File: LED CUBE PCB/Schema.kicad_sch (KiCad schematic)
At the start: 4 parts

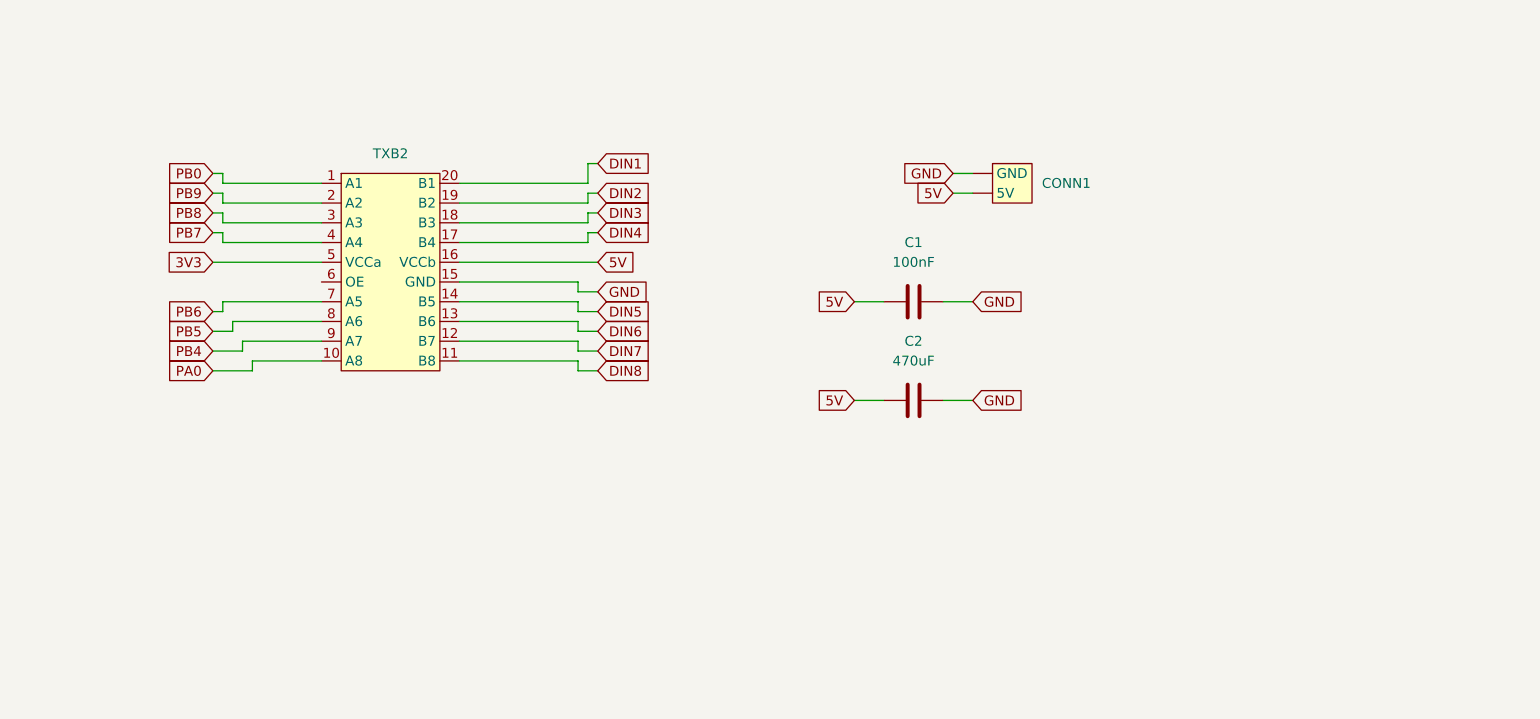
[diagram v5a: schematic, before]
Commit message: Corrected schema after review by Borna (Marina)
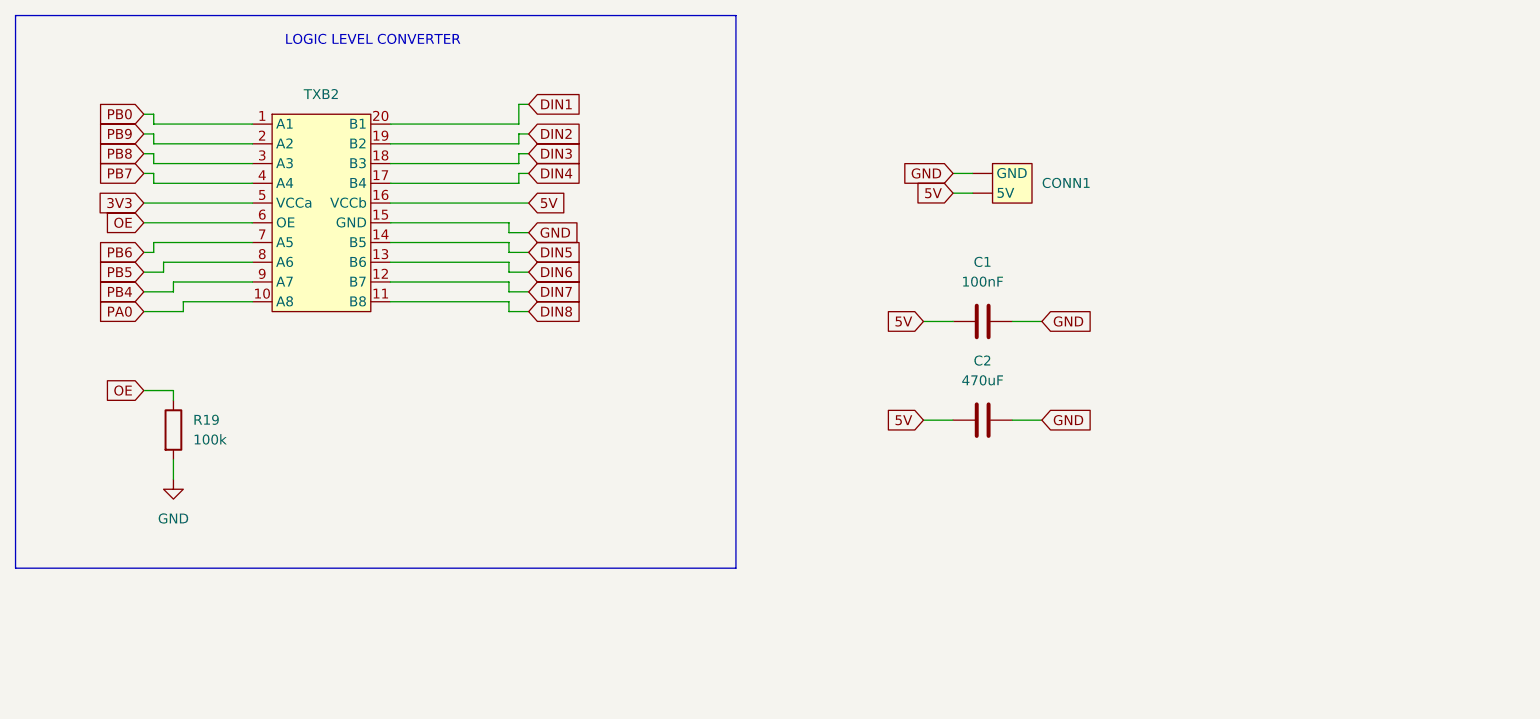
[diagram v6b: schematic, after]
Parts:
- added R19: 100k, BornaKiCad:R0603, symbol Device:R
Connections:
- net GND: now also R19.2
- net OE: now reaches TXB2.6 (OE)
- net OE: now also R19.1
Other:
- note added: "LOGIC LEVEL CONVERTER"
- moved on the sheet: C1, C2, TXB2

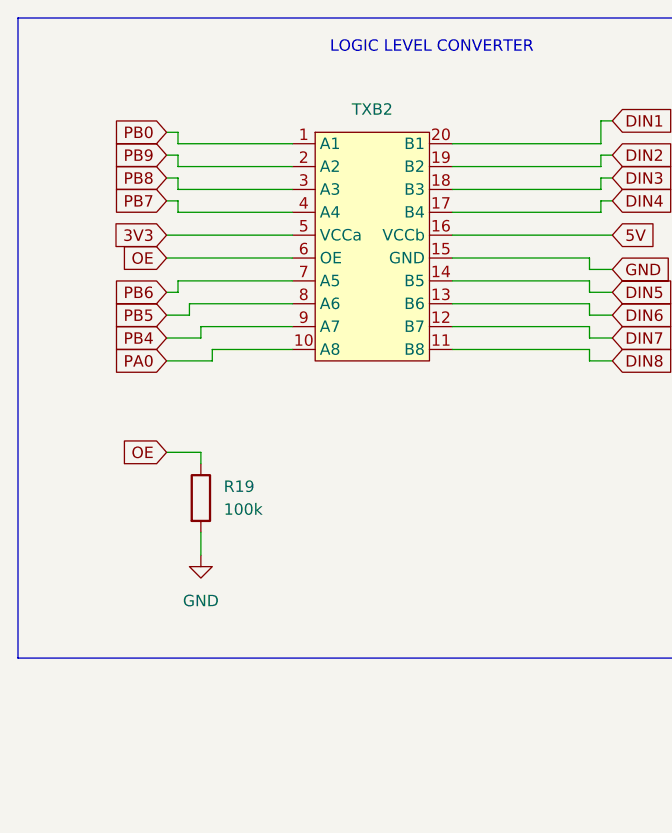
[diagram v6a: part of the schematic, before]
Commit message: Replaced symbol for TXB and STM
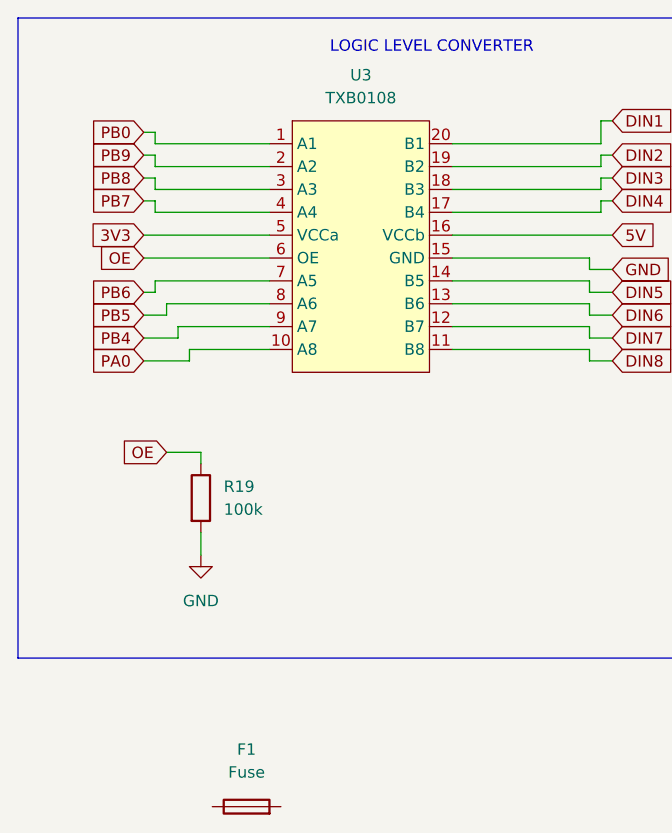
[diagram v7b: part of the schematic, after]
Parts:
- removed TXB2: ~, TXB0108:TXB0108, symbol TXB0108:TXB0108
- added F1: Fuse, symbol Device:Fuse
- added U3: TXB0108, TXB0108:TXB0108, symbol Marina_Library:TXB0108
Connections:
- net 3V3: now also U3.5 (VCCa)
- net 5V: now also U3.16 (VCCb)
- net DIN1: now also U3.20 (B1)
- net DIN2: now also U3.19 (B2)
- net DIN3: now also U3.18 (B3)
- net DIN4: now also U3.17 (B4)
- net DIN5: now also U3.14 (B5)
- net DIN6: now also U3.13 (B6)
- net DIN7: now also U3.12 (B7)
- net DIN8: now also U3.11 (B8)
- net GND: now also U3.15 (GND)
- net OE: now also U3.6 (OE)
- net PA0: now also U3.10 (A8)
- net PB0: now also U3.1 (A1)
- net PB4: now also U3.9 (A7)
- net PB5: now also U3.8 (A6)
- net PB6: now also U3.7 (A5)
- net PB7: now also U3.4 (A4)
- net PB8: now also U3.3 (A3)
- net PB9: now also U3.2 (A2)

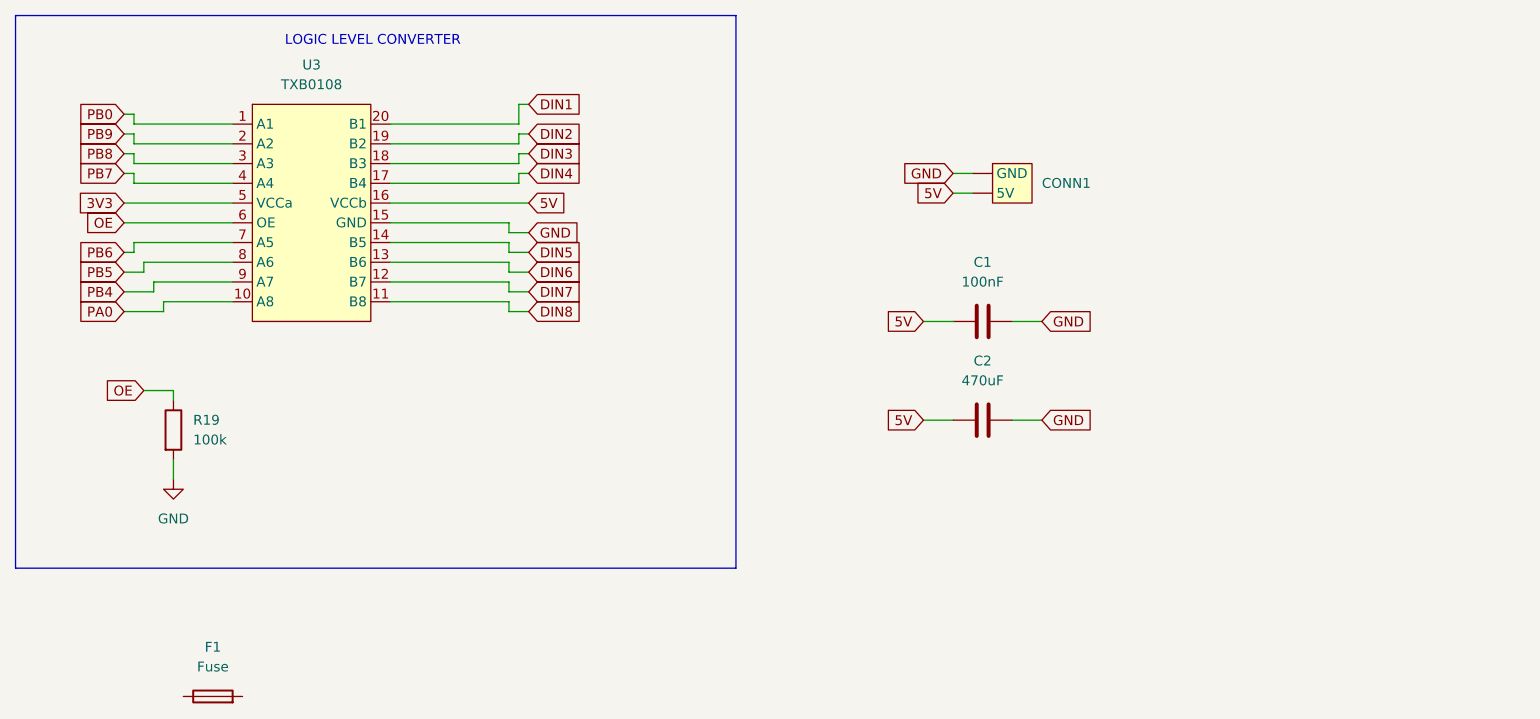
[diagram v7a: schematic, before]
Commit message: Added fuse and bat20
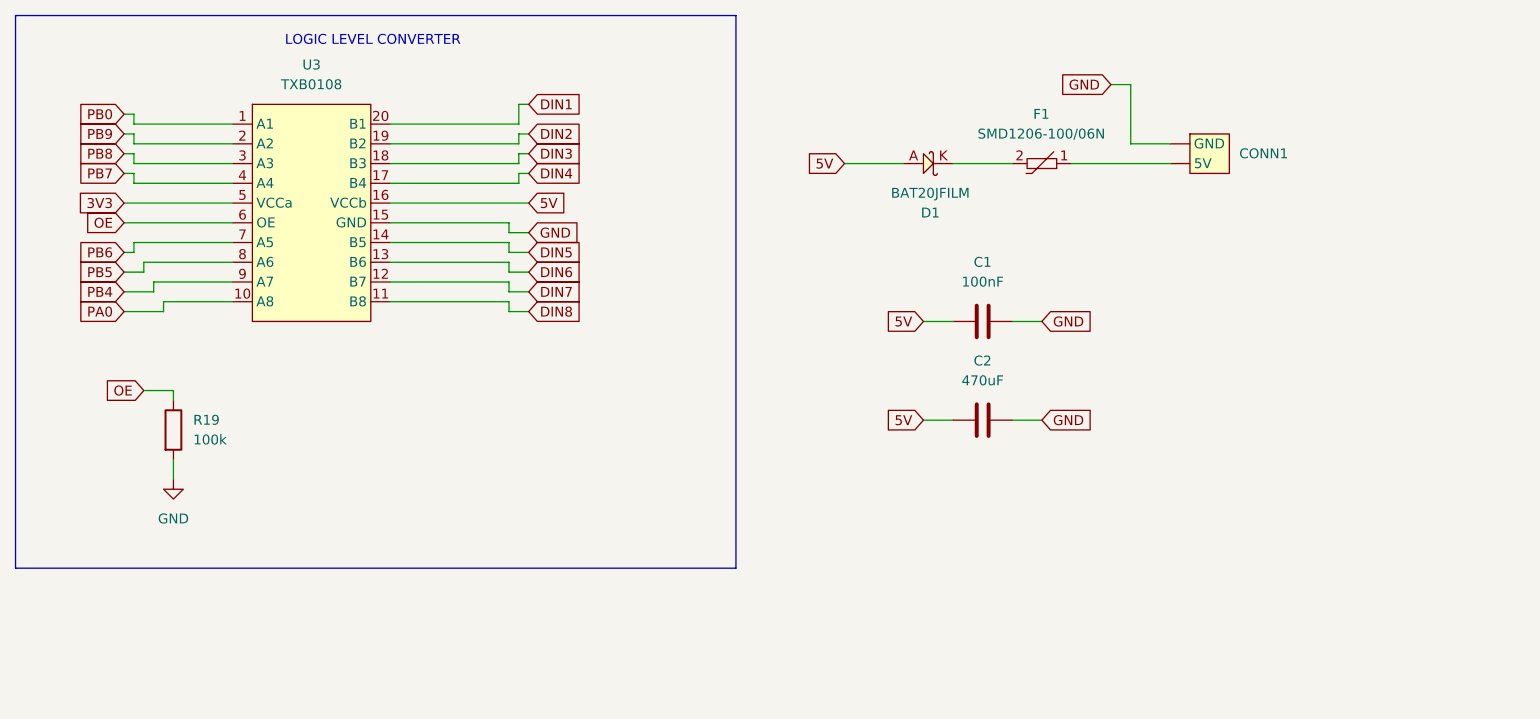
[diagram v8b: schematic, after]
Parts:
- removed F1: Fuse, symbol Device:Fuse
- added D1: BAT20JFILM, Borna KiCAD Library:SOD323, symbol Borna KiCAD Library:BAT20JFILM
- added F1: SMD1206-100/06N, Borna KiCAD Library:1206, symbol Borna KiCAD Library:SMD1206-100/06N
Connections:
- net 5V: now also D1.A; no longer CONN1. (GND)
- new net: D1.K, F1.2
- new net: CONN1. (GND), F1.1
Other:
- moved on the sheet: CONN1
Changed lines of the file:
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@@
+	(wire
+		(pts
+			(xy 160.02 30.48) (xy 160.02 22.86)
+		)
+		(stroke
+			(width 0)
+			(type default)
+		)
+	)
 	(wire
 		(pts
@@
 	(wire
 		(pts
-			(xy 137.16 36.83) (xy 139.7 36.83)
+			(xy 160.02 22.86) (xy 157.48 22.86)
 		)
 		(stroke
@@
 	(wire
 		(pts
+			(xy 160.02 30.48) (xy 165.1 30.48)
+		)
+		(stroke
+			(width 0)
+			(type default)
+		)
+	)
+	(wire
+		(pts
 			(xy 30.48 52.07) (xy 35.56 52.07)
 		)
@@
 	(wire
 		(pts
+			(xy 152.4 33.02) (xy 165.1 33.02)
+		)
+		(stroke
+			(width 0)
+			(type default)
+		)
+	)
+	(wire
+		(pts
 			(xy 36.83 62.23) (xy 36.83 63.5)
 		)
@@
 	(wire
 		(pts
+			(xy 123.19 33.02) (xy 130.81 33.02)
+		)
+		(stroke
+			(width 0)
+			(type default)
+		)
+	)
+	(wire
+		(pts
 			(xy 44.45 30.48) (xy 31.75 30.48)
 		)
@@
 	(wire
 		(pts
+			(xy 137.16 33.02) (xy 144.78 33.02)
+		)
+		(stroke
+			(width 0)
+			(type default)
+		)
+	)
+	(wire
+		(pts
 			(xy 44.45 50.8) (xy 35.56 50.8)
 		)
@@
 	(wire
 		(pts
-			(xy 137.16 34.29) (xy 139.7 34.29)
-		)
-		(stroke
-			(width 0)
-			(type default)
-		)
-	)
-	(wire
-		(pts
 			(xy 31.75 43.18) (xy 31.75 44.45)
 		)
@@
 	(global_label "5V"
 		(shape input)
-		(at 137.16 36.83 180)
+		(at 123.19 33.02 180)
 		(fields_autoplaced yes)
 		(effects
@@
 		)
 		(property "Intersheetrefs" "${INTERSHEET_REFS}"
-			(at 131.8767 36.83 0)
+			(at 117.9067 33.02 0)
 			(effects
 				(font
@@
 	(global_label "GND"
 		(shape input)
-		(at 137.16 34.29 180)
+		(at 157.48 22.86 180)
 		(fields_autoplaced yes)
 		(effects
@@
 		)
 		(property "Intersheetrefs" "${INTERSHEET_REFS}"
-			(at 130.3043 34.29 0)
+			(at 150.6243 22.86 0)
 			(effects
 				(font
@@
 	)
 	(symbol
+		(lib_id "Borna KiCAD Library:BAT20JFILM")
+		(at 133.35 33.02 0)
+		(unit 1)
+		(exclude_from_sim no)
+		(in_bom yes)
+		(on_board yes)
+		(dnp no)
+		(property "Reference" "D1"
+			(at 134.239 39.37 0)
+			(effects
+				(font
+					(size 1.27 1.27)
+				)
+			)
+		)
+		(property "Value" "BAT20JFILM"
+			(at 134.239 36.83 0)
+			(effects
+				(font
+					(size 1.27 1.27)
+				)
+			)
+		)
+		(property "Footprint" "Borna KiCAD Library:SOD323"
+			(at 133.35 33.02 0)
+			(effects
+				(font
+					(size 1.27 1.27)
+				)
+				(hide yes)
+			)
+		)
+		(property "Datasheet" ""
+			(at 133.35 33.02 0)
+			(effects
+				(font
+					(size 1.27 1.27)
+				)
+				(hide yes)
+			)
+		)
+		(property "Description" ""
+			(at 133.35 33.02 0)
+			(effects
+				(font
+					(size 1.27 1.27)
+				)
+				(hide yes)
+			)
+		)
+		(pin "A"
+		)
+		(pin "K"
+		)
+		(instances
+			(project ""
+				(path "/64eb2d32-222b-4351-90b6-2cc90b760e62/d4d78a1a-9980-4f28-b2ad-daf3a6ea4163"
+					(reference "D1")
+					(unit 1)
+				)
+			)
+		)
+	)
+	(symbol
 		(lib_id "Device:C")
 		(at 140.97 66.04 270)
@@
 				(path "/64eb2d32-222b-4351-90b6-2cc90b760e62/d4d78a1a-9980-4f28-b2ad-daf3a6ea4163"
 					(reference "C2")
+					(unit 1)
+				)
+			)
+		)
+	)
+	(symbol
+		(lib_id "Borna KiCAD Library:SMD1206-100/06N")
+		(at 148.59 33.02 180)
+		(unit 1)
+		(exclude_from_sim no)
+		(in_bom yes)
+		(on_board yes)
+		(dnp no)
+		(fields_autoplaced yes)
+		(property "Reference" "F1"
+			(at 148.5265 26.67 0)
+			(effects
+				(font
+					(size 1.27 1.27)
+				)
+			)
+		)
+		(property "Value" "SMD1206-100/06N"
+			(at 148.5265 29.21 0)
+			(effects
+				(font
+					(size 1.27 1.27)
+				)
+			)
+		)
+		(property "Footprint" "Borna KiCAD Library:1206"
+			(at 148.59 26.924 0)
+			(effects
+				(font
+					(size 1.27 1.27)
+				)
+				(hide yes)
+			)
+		)
+		(property "Datasheet" ""
+			(at 148.59 33.02 0)
+			(effects
+				(font
+					(size 1.27 1.27)
+				)
+				(hide yes)
+			)
+		)
+		(property "Description" ""
+			(at 148.59 33.02 0)
+			(effects
+				(font
+					(size 1.27 1.27)
+				)
+				(hide yes)
+			)
+		)
+		(pin "1"
+		)
+		(pin "2"
+		)
+		(instances
+			(project ""
+				(path "/64eb2d32-222b-4351-90b6-2cc90b760e62/d4d78a1a-9980-4f28-b2ad-daf3a6ea4163"
+					(reference "F1")
 					(unit 1)
 				)
@@
 	)
 	(symbol
-		(lib_id "Device:Fuse")
-		(at 41.91 101.6 90)
+		(lib_id "POWER_SUPPLY:U")
+		(at 170.18 31.75 0)
 		(unit 1)
 		(exclude_from_sim no)
@@
 		(dnp no)
 		(fields_autoplaced yes)
-		(property "Reference" "F1"
-			(at 41.91 95.25 90)
-			(effects
-				(font
-					(size 1.27 1.27)
-				)
-			)
-		)
-		(property "Value" "Fuse"
-			(at 41.91 97.79 90)
-			(effects
-				(font
-					(size 1.27 1.27)
-				)
-			)
-		)
-		(property "Footprint" ""
-			(at 41.91 103.378 90)
-			(effects
-				(font
-					(size 1.27 1.27)
-				)
-				(hide yes)
-			)
-		)
-		(property "Datasheet" "~"
-			(at 41.91 101.6 0)
-			(effects
-				(font
-					(size 1.27 1.27)
-				)
-				(hide yes)
-			)
-		)
-		(property "Description" "Fuse"
-			(at 41.91 101.6 0)
-			(effects
-				(font
-					(size 1.27 1.27)
-				)
-				(hide yes)
-			)
-		)
-		(pin "2"
-		)
-		(pin "1"
-		)
-		(instances
-			(project ""
-				(path "/64eb2d32-222b-4351-90b6-2cc90b760e62/d4d78a1a-9980-4f28-b2ad-daf3a6ea4163"
-					(reference "F1")
-					(unit 1)
-				)
-			)
-		)
-	)
-	(symbol
-		(lib_id "POWER_SUPPLY:U")
-		(at 144.78 35.56 0)
-		(unit 1)
-		(exclude_from_sim no)
-		(in_bom yes)
-		(on_board yes)
-		(dnp no)
-		(fields_autoplaced yes)
 		(property "Reference" "CONN1"
-			(at 148.59 35.5599 0)
+			(at 173.99 31.7499 0)
 			(effects
 				(font
@@
 		)
 		(property "Value" "POWER_SUPPLY"
-			(at 144.78 41.402 0)
+			(at 170.18 37.592 0)
 			(effects
 				(font
@@
 		)
 		(property "Footprint" "Connector_PinSocket_2.54mm:PinSocket_1x02_P2.54mm_Vertical"
-			(at 144.78 39.37 0)
+			(at 170.18 35.56 0)
 			(effects
 				(font
@@
 		)
 		(property "Datasheet" ""
-			(at 144.78 35.56 0)
+			(at 170.18 31.75 0)
 			(effects
 				(font
@@
 		)
 		(property "Description" ""
-			(at 144.78 35.56 0)
-			(effects
-				(font
+			(at 170.18 31.75 0)
+			(effects
+				(font
